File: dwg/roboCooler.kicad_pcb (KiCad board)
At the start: 2 copper layers, 39 parts, among them J1 CONN_02X25, J10 CONN_01X12, J11 CONN_01X12, J2 CONN_02X25, J3 CONN_01X04, J5 CONN_01X02, J7 CONN_01X02, J9 CONN_01X06, Q1 NMOS, Q2 NMOS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

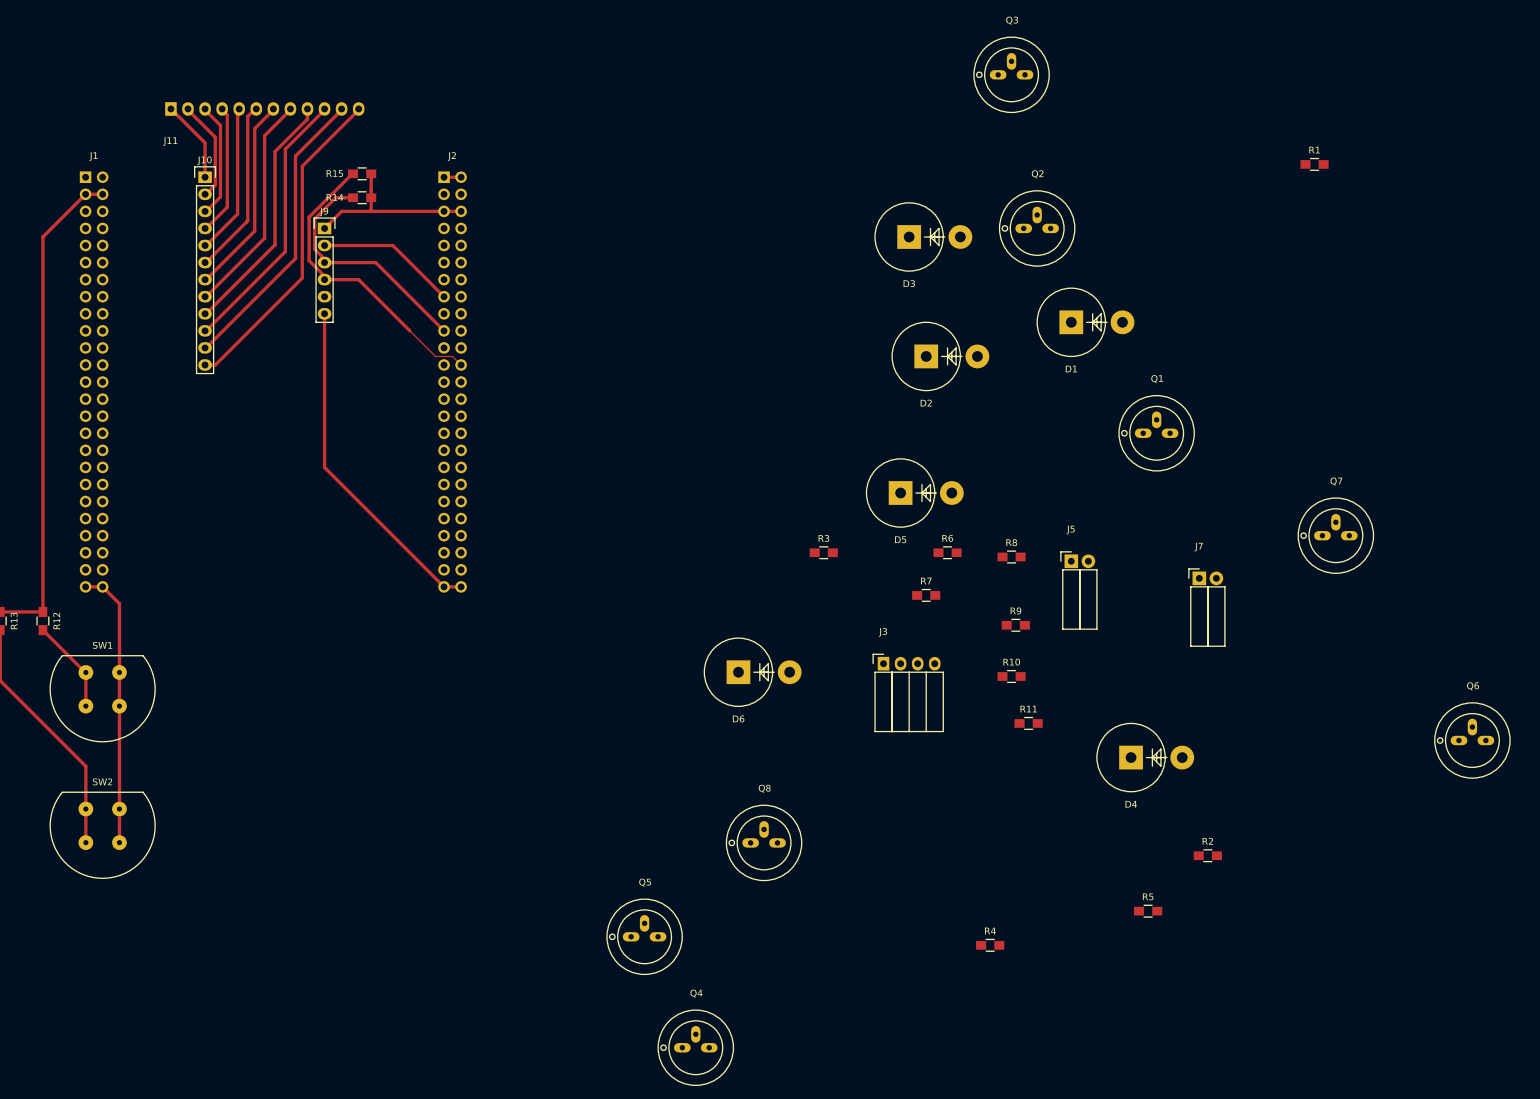
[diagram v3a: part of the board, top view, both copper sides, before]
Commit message: Added LED USART to layout
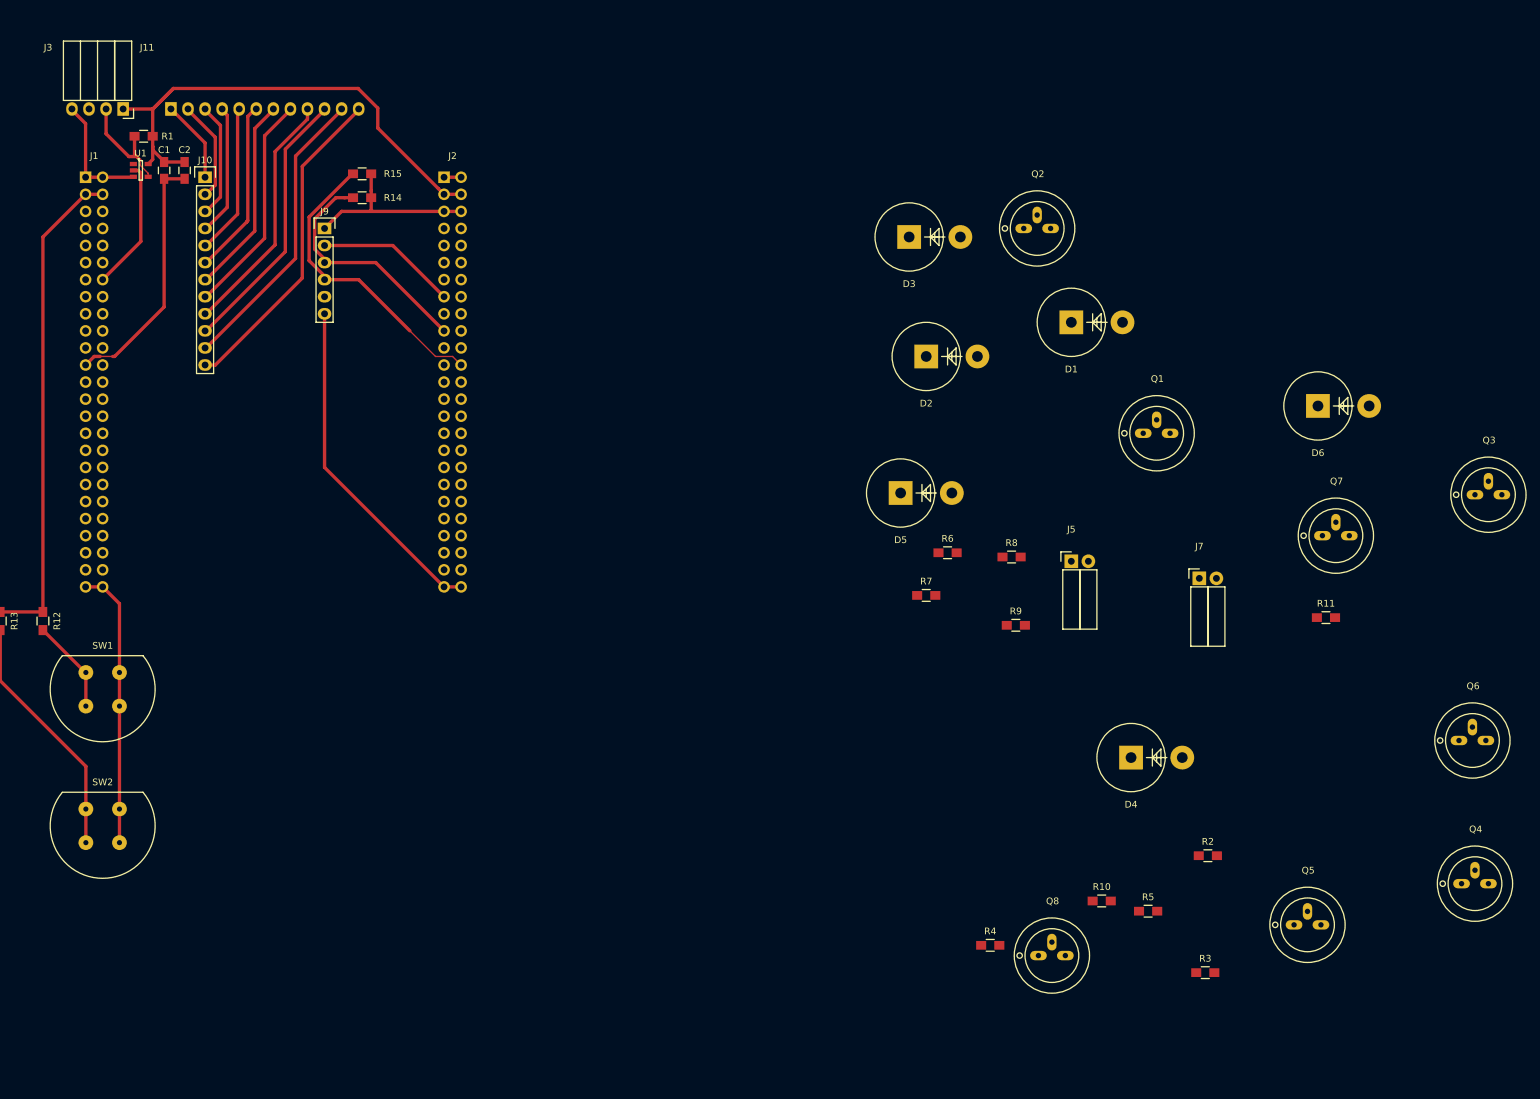
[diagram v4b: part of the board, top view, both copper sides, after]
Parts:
- added C1: .01UF, Capacitors_SMD:C_0805_HandSoldering, F.Cu at (75.2, 39.6)
- added C2: 1UF, Capacitors_SMD:C_0805_HandSoldering, F.Cu at (78.2, 39.6)
- added U1: SN74LV, TO_SOT_Packages_SMD:SOT-23-5, F.Cu at (71.7, 39.6)
- moved R1 174.3 mm to (72.1, 34.5), turned to 180 degrees
- moved J3 140.1 mm to (69.1, 30.5), turned to 180 degrees
- moved Q4 118.5 mm to (270.3, 145.8)
- moved Q5 98.7 mm to (245.3, 151.9)
- moved D6 94.9 mm to (246.9, 74.7)
- moved Q3 94.6 mm to (272.3, 87.9)
- moved R3 84.4 mm to (230.1, 159.0)
- moved R11 47.0 mm to (248.1, 106.2)
- moved Q8 46.0 mm to (207.3, 156.5)
- moved R10 36.0 mm to (214.7, 148.3)
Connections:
- J1 pad 14: Net-(J1-Pad14) -> LED_UART
- J2 pad 21: LED_UART -> Net-(J2-Pad21)
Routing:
- net +5V: track 0.00 -> 78.8 mm
- net POWER_GND: track 94.8 -> 150.3 mm
- net LED_UART: track 0.00 -> 19.5 mm
- net Net-(J3-Pad2): track 0.00 -> 16.5 mm

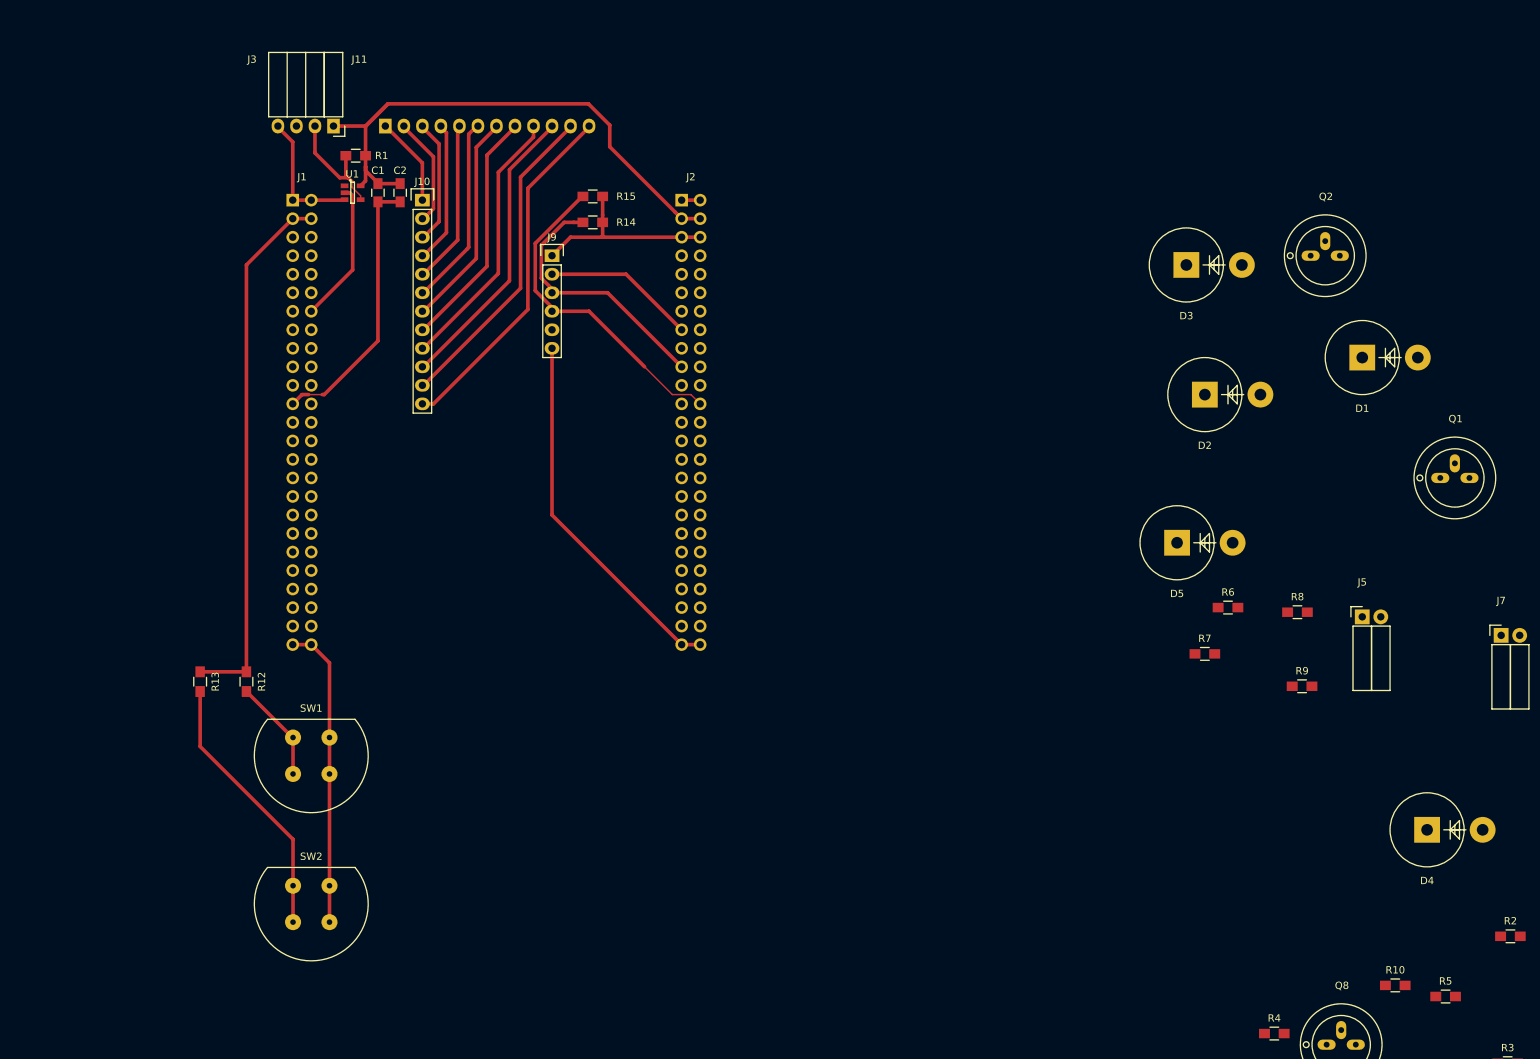
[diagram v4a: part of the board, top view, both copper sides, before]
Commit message: added fan driver components to layout
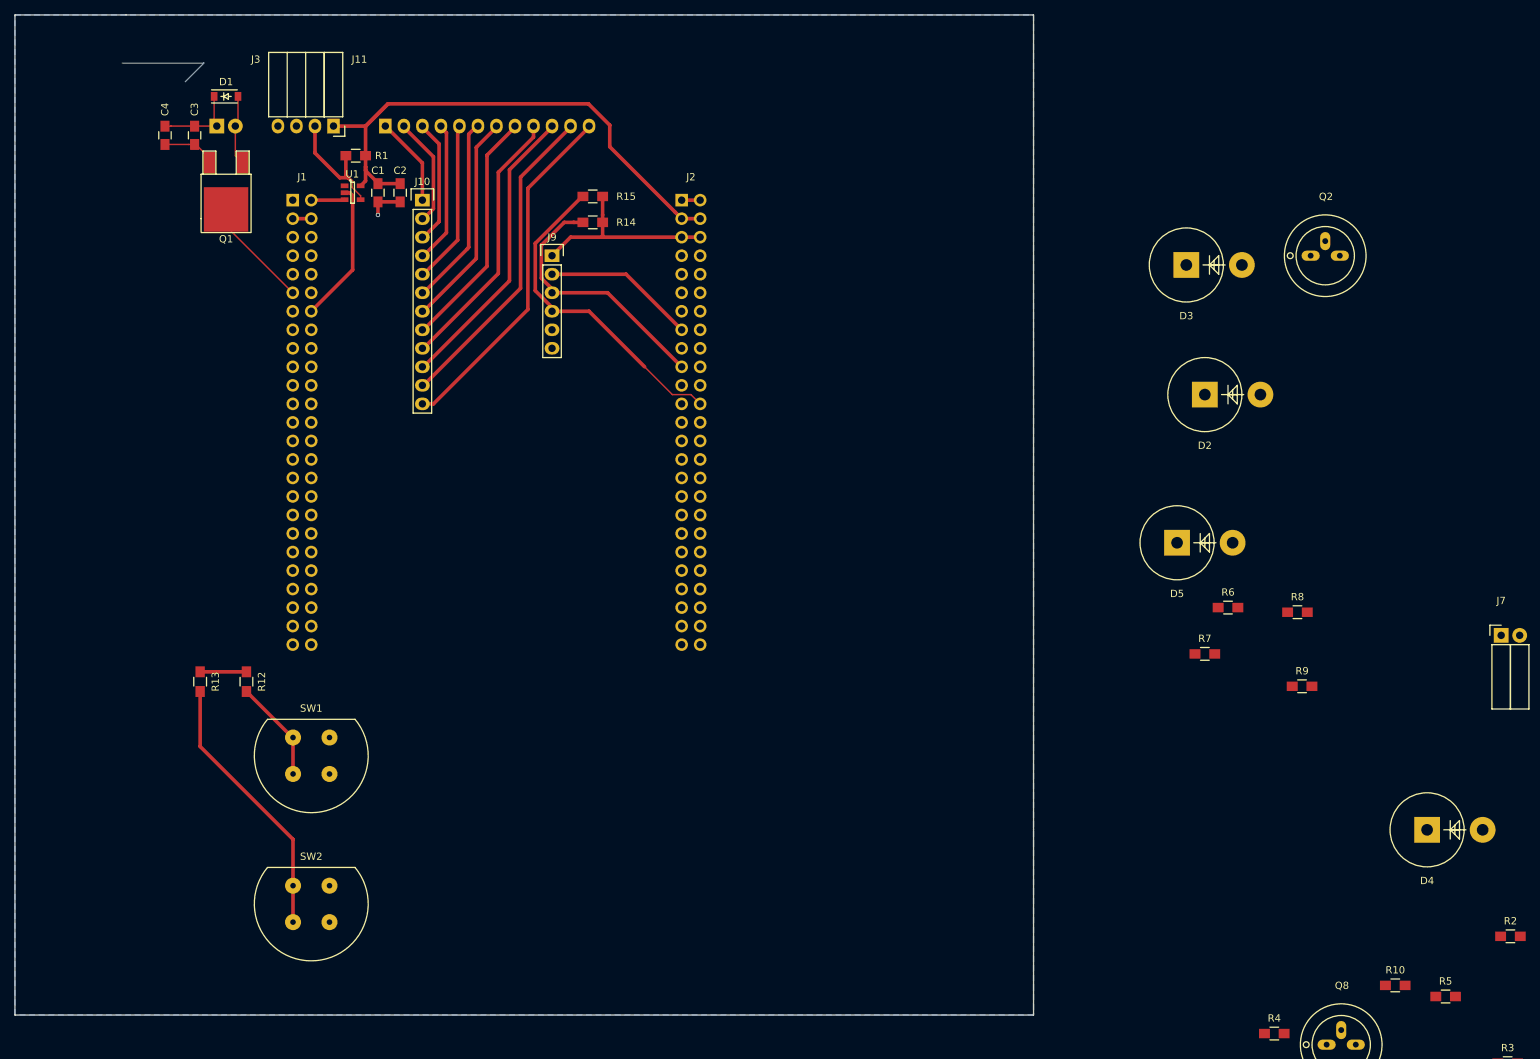
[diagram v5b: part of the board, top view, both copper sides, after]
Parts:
- added C3: .01UF, Capacitors_SMD:C_0805_HandSoldering, F.Cu at (50.0, 31.8)
- added C4: 1UF, Capacitors_SMD:C_0805_HandSoldering, F.Cu at (46.0, 31.8)
- D1: value D_Schottky_Small -> BAT42; footprint Diodes_ThroughHole:Diode_P600_Vertical_AnodeUp -> Diodes_SMD:SOD-123
- J5: moved to B.Cu
- Q1: footprint Transistors_OldSowjetAera:OldSowjetaera_Transistor_Type-II_BigPads -> TO_SOT_Packages_SMD:TO-252-2Lead
- moved Q1 174.0 mm to (54.4, 35.6), turned to 180 degrees
- moved J5 170.9 mm to (53.1, 30.5)
- moved D1 159.9 mm to (54.4, 26.4)
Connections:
- J1 pad 11: Net-(J1-Pad11) -> FAN
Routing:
- net POWER_GND: track 150.3 -> 19.8 mm, vias 0 -> 1
- net VDD: track 73.7 -> 8.89 mm
- net FAN: track 0.00 -> 15.2 mm
- net (no net): track 0.00 -> 14.8 mm
- net +12V: track 0.00 -> 11.3 mm
- net Net-(D1-Pad2): track 0.00 -> 9.94 mm
- added copper zone on B.Cu, net POWER_GND
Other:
- board outline added: 139.7 x 137.2 mm

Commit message: fixed cap sense conn gender footprint
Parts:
- J9: footprint Pin_Headers:Pin_Header_Straight_1x06 -> Socket_Strips:Socket_Strip_Straight_1x06
- turned J9 to 270 degrees
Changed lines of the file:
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@@
   (general
     (links 103)
-    (no_connects 46)
+    (no_connects 48)
     (area 25.349999 15.189999 165.150001 152.450001)
     (thickness 1.6)
@@
       (net 8 POWER_GND))
   )
-  (module Pin_Headers:Pin_Header_Straight_1x06 (layer F.Cu)
-    (at 99.06 48.26)
-    (descr "Through hole pin header")
-    (tags "pin header")
-    (fp_text reference J9 (at 0 -2.54) (layer F.SilkS)
-      (effects (font (size 1 1) (thickness 0.15)))
-    )
-    (fp_text value CONN_01X06 (at 0 15.24) (layer F.Fab)
-      (effects (font (size 1 1) (thickness 0.15)))
-    )
-    (fp_line (start -1.75 -1.75) (end -1.75 14.45) (layer F.CrtYd) (width 0.05))
-    (fp_line (start 1.75 -1.75) (end 1.75 14.45) (layer F.CrtYd) (width 0.05))
-    (fp_line (start -1.75 -1.75) (end 1.75 -1.75) (layer F.CrtYd) (width 0.05))
-    (fp_line (start -1.75 14.45) (end 1.75 14.45) (layer F.CrtYd) (width 0.05))
-    (fp_line (start 1.27 1.27) (end 1.27 13.97) (layer F.SilkS) (width 0.15))
-    (fp_line (start 1.27 13.97) (end -1.27 13.97) (layer F.SilkS) (width 0.15))
-    (fp_line (start -1.27 13.97) (end -1.27 1.27) (layer F.SilkS) (width 0.15))
-    (fp_line (start 1.55 -1.55) (end 1.55 0) (layer F.SilkS) (width 0.15))
-    (fp_line (start 1.27 1.27) (end -1.27 1.27) (layer F.SilkS) (width 0.15))
-    (fp_line (start -1.55 0) (end -1.55 -1.55) (layer F.SilkS) (width 0.15))
-    (fp_line (start -1.55 -1.55) (end 1.55 -1.55) (layer F.SilkS) (width 0.15))
-    (pad 1 thru_hole rect (at 0 0) (size 2.032 1.7272) (drill 1.016) (layers *.Cu *.Mask F.SilkS)
-      (net 47 +3V3))
-    (pad 2 thru_hole oval (at 0 2.54) (size 2.032 1.7272) (drill 1.016) (layers *.Cu *.Mask F.SilkS)
-      (net 85 CS_IRQ))
-    (pad 3 thru_hole oval (at 0 5.08) (size 2.032 1.7272) (drill 1.016) (layers *.Cu *.Mask F.SilkS)
-      (net 59 CS_SCL))
-    (pad 4 thru_hole oval (at 0 7.62) (size 2.032 1.7272) (drill 1.016) (layers *.Cu *.Mask F.SilkS)
-      (net 63 CS_SDA))
-    (pad 5 thru_hole oval (at 0 10.16) (size 2.032 1.7272) (drill 1.016) (layers *.Cu *.Mask F.SilkS)
-      (net 118 "Net-(J9-Pad5)"))
-    (pad 6 thru_hole oval (at 0 12.7) (size 2.032 1.7272) (drill 1.016) (layers *.Cu *.Mask F.SilkS)
-      (net 8 POWER_GND))
-    (model Pin_Headers.3dshapes/Pin_Header_Straight_1x06.wrl
-      (at (xyz 0 -0.25 0))
-      (scale (xyz 1 1 1))
-      (rotate (xyz 0 0 90))
-    )
-  )
   (module Resistors_SMD:R_0805_HandSoldering (layer F.Cu)
     (at 104.648 43.688 180)
@@
       (net 1 "Net-(D1-Pad2)"))
   )
+  (module Socket_Strips:Socket_Strip_Straight_1x06 (layer F.Cu)
+    (at 99.06 48.26 270)
+    (descr "Through hole socket strip")
+    (tags "socket strip")
+    (fp_text reference J9 (at 0 -5.1 270) (layer F.SilkS)
+      (effects (font (size 1 1) (thickness 0.15)))
+    )
+    (fp_text value CONN_01X06 (at 0 -3.1 270) (layer F.Fab)
+      (effects (font (size 1 1) (thickness 0.15)))
+    )
+    (fp_line (start -1.75 -1.75) (end -1.75 1.75) (layer F.CrtYd) (width 0.05))
+    (fp_line (start 14.45 -1.75) (end 14.45 1.75) (layer F.CrtYd) (width 0.05))
+    (fp_line (start -1.75 -1.75) (end 14.45 -1.75) (layer F.CrtYd) (width 0.05))
+    (fp_line (start -1.75 1.75) (end 14.45 1.75) (layer F.CrtYd) (width 0.05))
+    (fp_line (start 1.27 1.27) (end 13.97 1.27) (layer F.SilkS) (width 0.15))
+    (fp_line (start 13.97 1.27) (end 13.97 -1.27) (layer F.SilkS) (width 0.15))
+    (fp_line (start 13.97 -1.27) (end 1.27 -1.27) (layer F.SilkS) (width 0.15))
+    (fp_line (start -1.55 1.55) (end 0 1.55) (layer F.SilkS) (width 0.15))
+    (fp_line (start 1.27 1.27) (end 1.27 -1.27) (layer F.SilkS) (width 0.15))
+    (fp_line (start 0 -1.55) (end -1.55 -1.55) (layer F.SilkS) (width 0.15))
+    (fp_line (start -1.55 -1.55) (end -1.55 1.55) (layer F.SilkS) (width 0.15))
+    (pad 1 thru_hole rect (at 0 0 270) (size 1.7272 2.032) (drill 1.016) (layers *.Cu *.Mask F.SilkS)
+      (net 47 +3V3))
+    (pad 2 thru_hole oval (at 2.54 0 270) (size 1.7272 2.032) (drill 1.016) (layers *.Cu *.Mask F.SilkS)
+      (net 85 CS_IRQ))
+    (pad 3 thru_hole oval (at 5.08 0 270) (size 1.7272 2.032) (drill 1.016) (layers *.Cu *.Mask F.SilkS)
+      (net 59 CS_SCL))
+    (pad 4 thru_hole oval (at 7.62 0 270) (size 1.7272 2.032) (drill 1.016) (layers *.Cu *.Mask F.SilkS)
+      (net 63 CS_SDA))
+    (pad 5 thru_hole oval (at 10.16 0 270) (size 1.7272 2.032) (drill 1.016) (layers *.Cu *.Mask F.SilkS)
+      (net 118 "Net-(J9-Pad5)"))
+    (pad 6 thru_hole oval (at 12.7 0 270) (size 1.7272 2.032) (drill 1.016) (layers *.Cu *.Mask F.SilkS)
+      (net 8 POWER_GND))
+    (model Socket_Strips.3dshapes/Socket_Strip_Straight_1x06.wrl
+      (at (xyz 0.25 0 0))
+      (scale (xyz 1 1 1))
+      (rotate (xyz 0 0 180))
+    )
+  )
   (gr_line (start 25.4 15.24) (end 40.64 15.24) (layer Edge.Cuts) (width 0.1))
